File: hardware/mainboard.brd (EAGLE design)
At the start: 160 x 100 mm, 86 parts, among them IC1 ATMEGA328, IC10 HM628512A_DIL32, IC11 HM628512A_DIL32, IC12 7805TV, IC14 6N138, IC3 TL974, IC4 74HCT04N, IC5 74HC238N, IC6 74HCT573N, IC7 74HCT573N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

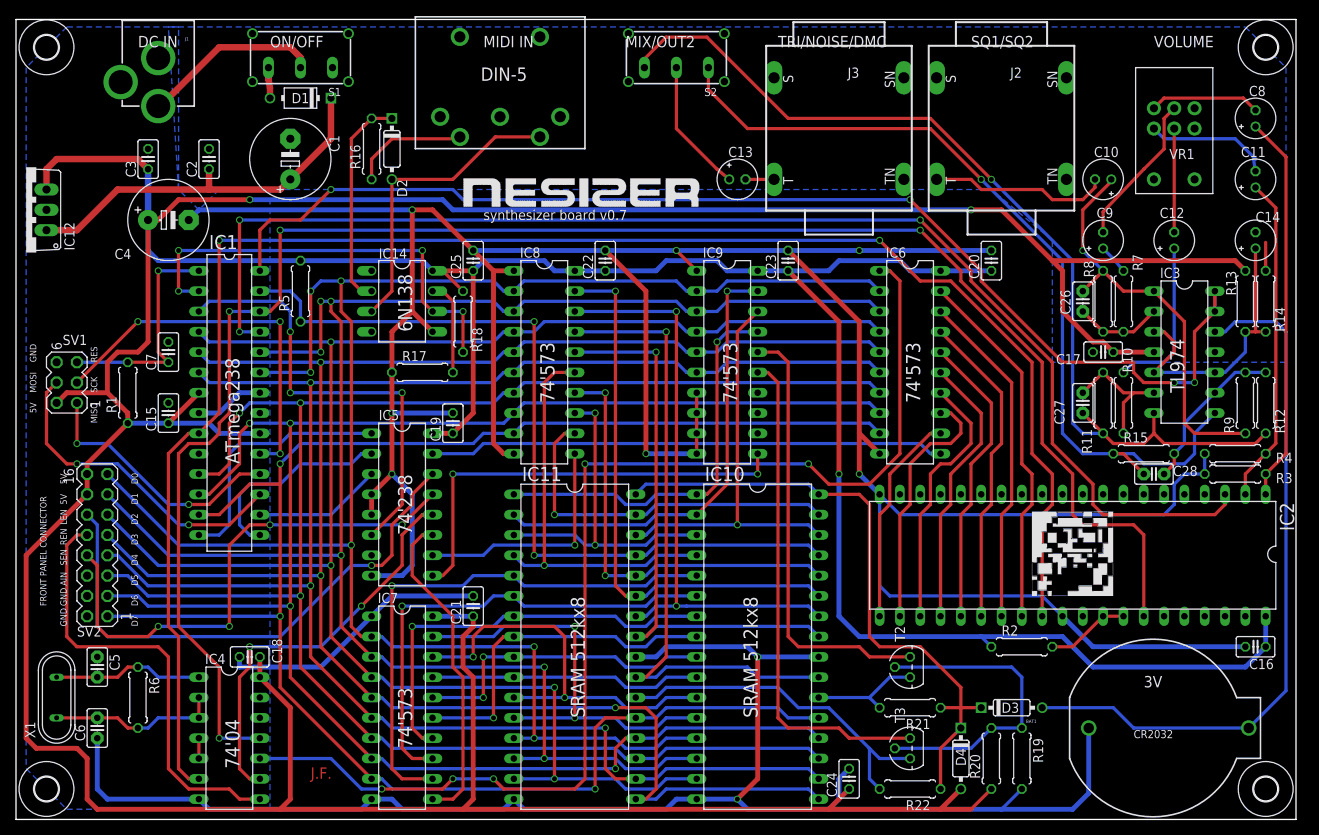
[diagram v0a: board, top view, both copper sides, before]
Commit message: Main board v0.9: fix memory backup, new MIDI connector, BOM fixes
The discrete memory backup circuit turned out to be too fragile. The old
DS1210 based design is back, but it is now also used to provide the CPU
RESET signal to further reduce the possibility of memory corruption. The
battery voltage is still being connected (through a buffer) to the
Atmega for being able to check the battery voltage.

The MIDI connector that was used previously is not being stocked at
Mouser any more, so it has been replaced by one that is.

A couple of fixes have been done to the BOM, replacing out of stock
components with drop-in replacements (a resistor and the 74'238).

This should hopefully be the last revision of the main board...
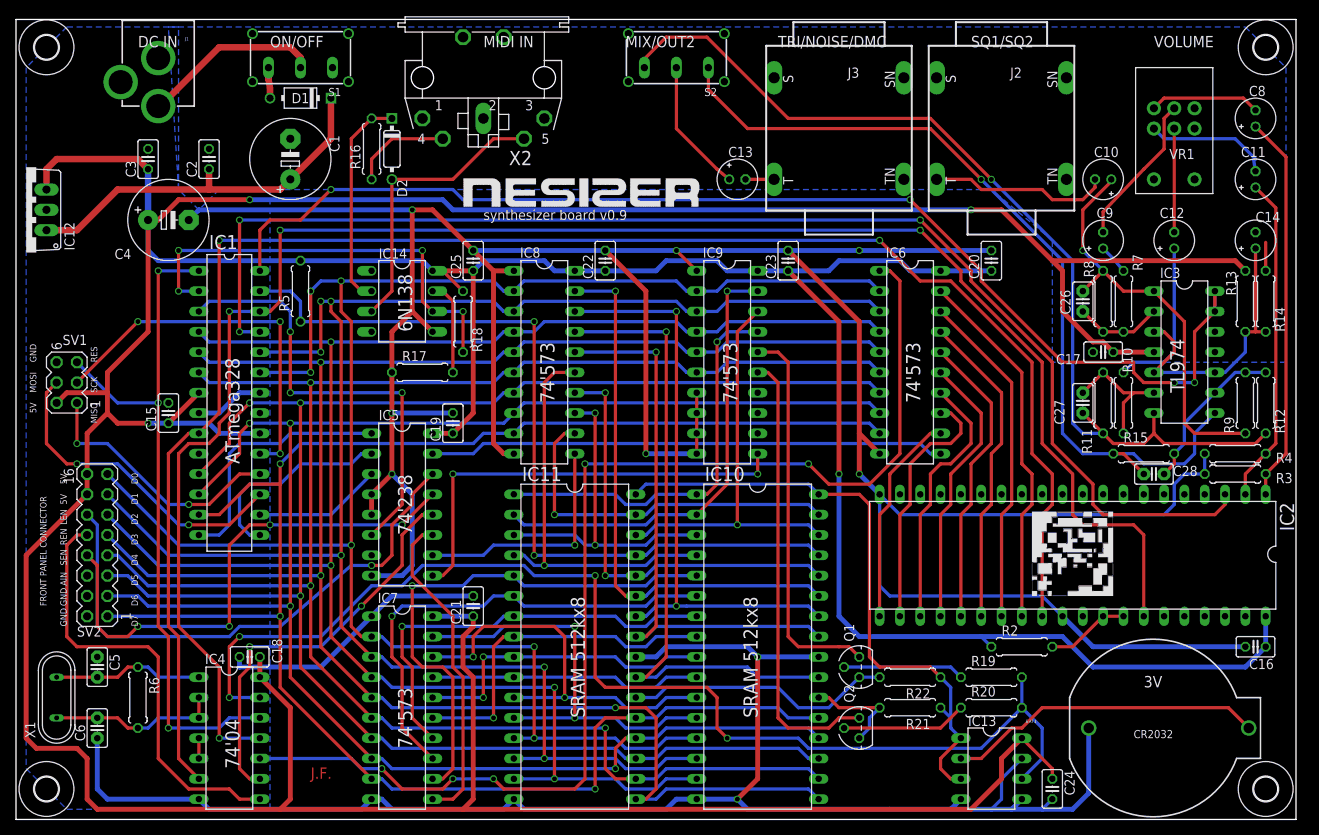
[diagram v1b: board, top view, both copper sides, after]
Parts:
- removed C7: 10n, rcl:C025-025X050
- removed D3, D4: 1N914.3, gm-diodes:DO35-3
- removed J4: MIDI_CONN_FEMALE_SUPPORT, SparkFun-Connectors:DIN_5_FEMALE_SUPPORT
- removed R1: 4.7k, rcl:0207/7
- removed T2, T3: BC547, transistor:TO92
- added IC13: DS1210-8PDIP, maxim-custom:DIL08
- added Q1, Q2: BC557, transistor-pnp:TO92
- added X2: MAB5SH, con-hirschmann:MAB5SH
- R19: value 4.7k -> 1k
- R20: value 27k -> 1k
- R21, R22: value 4.7k -> 100k
- moved C24 25.4 mm to (129.5, 3.81), turned to 270 degrees
- moved R22 14.0 mm to (111.8, 17.8)
- moved R19 10.9 mm to (121.9, 17.8), turned to 0 degrees
- moved R20 6.35 mm to (121.9, 14.0), turned to 0 degrees
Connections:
- removed net N$19: BAT1.1, D3.A, IC3.12
- new net N$37: Q1.2, R19.1
- new net N$38: Q2.2, R20.1
- new net N$39: BAT1.1, IC13.2, IC3.12
- net CE1: now also Q1.1; no longer T2.1
- net CE2: now also Q2.1; no longer T3.1
- net GND: now also IC13.4, IC13.5, IC13.7, X2.PE, X2.PE@; no longer C7.2, IC4.13, R19.2
- net MEM1_CE: now also Q2.3; no longer T2.3
- net MEM2_CE: now also Q1.3; no longer T3.3
- net MEM_VCC: now also IC13.1, IC13.3; no longer D3.C, D4.C
- net MIDI_PIN_4: now also X2.4; no longer J4.4
- net MIDI_PIN_5: now also X2.5; no longer J4.5
- net N$33: now also IC13.6, IC4.13, R19.2; no longer R19.1, T2.2, T3.2
- net RESET: now also IC4.12; no longer C7.1, R1.2
- net VCC: now also IC13.8; no longer D4.A, R1.1, R20.1
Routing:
- net N$33: track 39.7 -> 149.5 mm, vias 0 -> 4
- net N$19: track 88.3 -> 0.00 mm
- net RESET: track 28.5 -> 87.0 mm, vias 1 -> 3
- net N$39: track 0.00 -> 39.7 mm
- net N$38: track 0.00 -> 15.7 mm
- net N$37: track 0.00 -> 15.1 mm
- net MEM2_CE: track 44.1 -> 33.6 mm
- net VCC: track 727.0 -> 733.9 mm, vias 3 -> 4
- net CE2: track 62.5 -> 56.2 mm
- net CE1: track 54.9 -> 48.6 mm
- net GND: track 637.6 -> 641.2 mm
- net MIDI_PIN_4: track 14.7 -> 12.5 mm
- net MIDI_PIN_5: track 38.3 -> 36.2 mm
- net MEM_VCC: track 80.2 -> 78.2 mm
- net DB5: track 222.1 -> 220.6 mm
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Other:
- board text added: "ATmega328"
- board text added: "synthesizer board v0.9"
- board text removed: "ATmega238"
- board text removed: "synthesizer board v0.7"

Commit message: HW 0.9 fix
Added missing trace from battery to op-amp
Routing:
- net N$39: track 39.7 -> 88.1 mm, vias 0 -> 2
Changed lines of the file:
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@@
 <wire x1="128.27" y1="13.97" x2="151.55" y2="13.97" width="0.4064" layer="1"/>
 <wire x1="151.55" y1="13.97" x2="154.09" y2="11.43" width="0.4064" layer="1"/>
-<wire x1="151.55" y1="13.97" x2="149.86" y2="60.96" width="0" layer="19" extent="1-1"/>
+<wire x1="151.55" y1="13.97" x2="151.55" y2="22.01" width="0.4064" layer="1"/>
+<wire x1="151.55" y1="22.01" x2="152.4" y2="22.86" width="0.4064" layer="1"/>
+<wire x1="152.4" y1="22.86" x2="152.4" y2="45.72" width="0.4064" layer="1"/>
+<via x="152.4" y="45.72" extent="1-16" drill="0.6"/>
+<wire x1="152.4" y1="45.72" x2="152.4" y2="49.53" width="0.4064" layer="16"/>
+<via x="152.4" y="49.53" extent="1-16" drill="0.6"/>
+<wire x1="152.4" y1="49.53" x2="152.4" y2="58.42" width="0.4064" layer="1"/>
+<wire x1="152.4" y1="58.42" x2="149.86" y2="60.96" width="0.4064" layer="1"/>
 </signal>
 </signals>

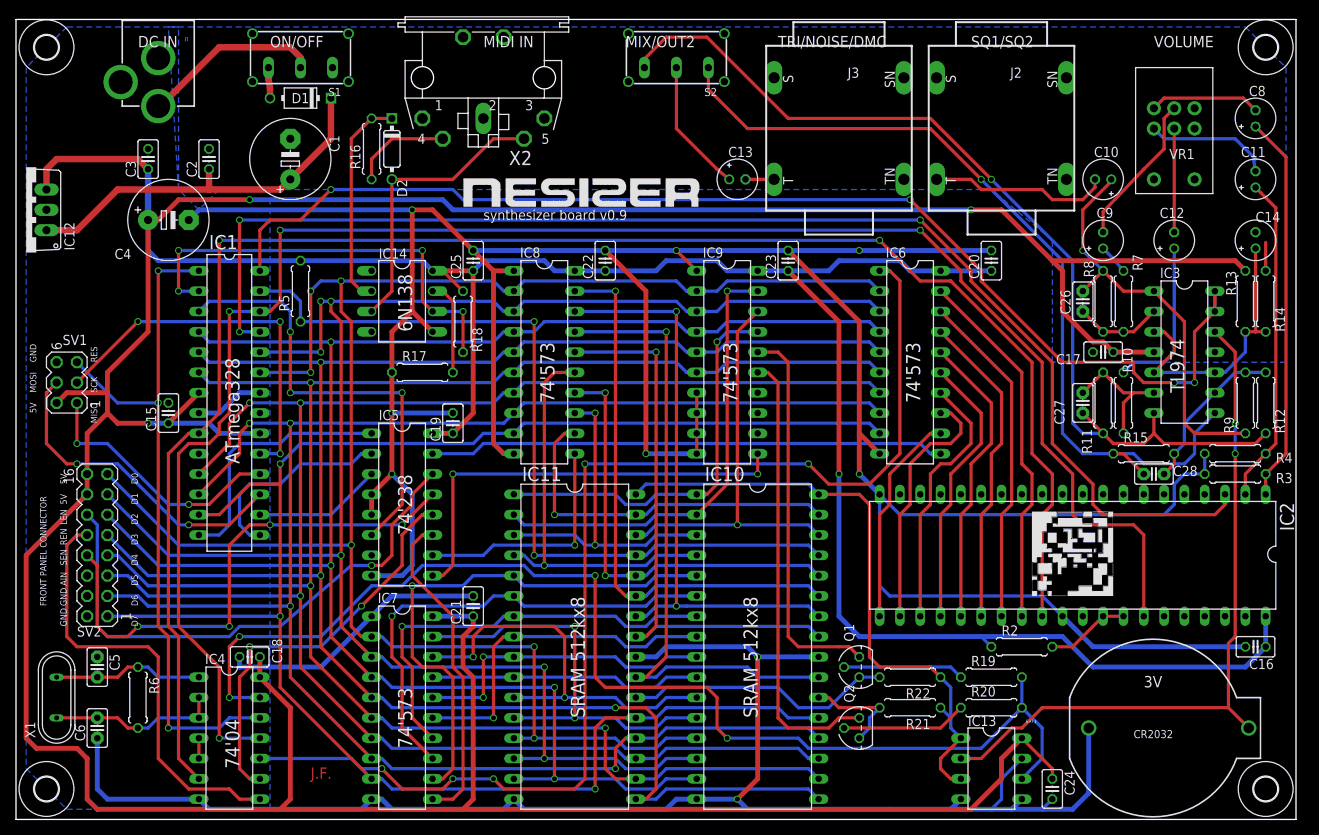
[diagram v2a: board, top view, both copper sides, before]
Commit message: HW: main board update
Fixes a few faults in the latest main board revision:

- Remove RESET connection from DS1210
- Add 10M resistor between battery and op-amp
        Eliminates leakage through op-amp inputs which would
        cause DS1210 to switch mode to "on".
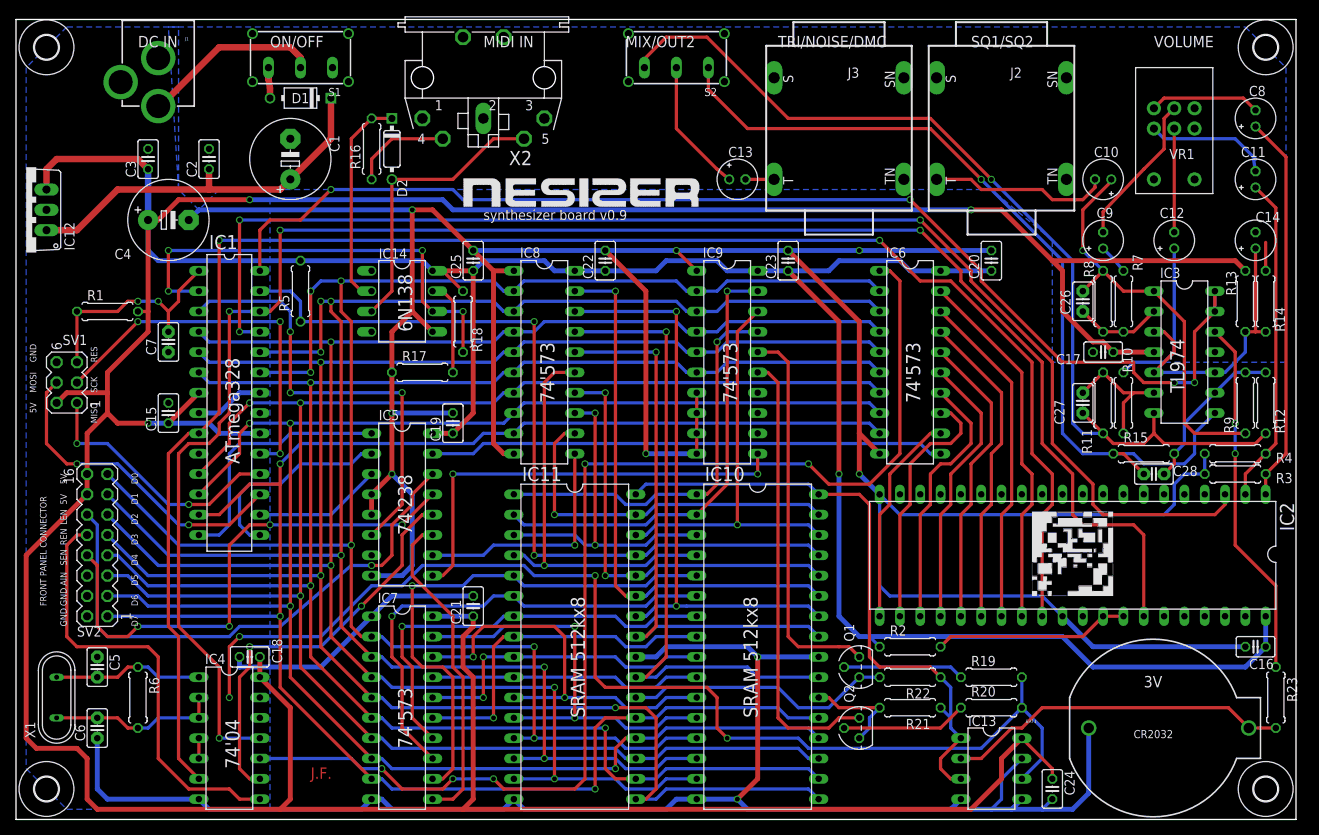
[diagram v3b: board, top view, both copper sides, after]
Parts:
- added C7: 10n, capacitor-wima:C2.5-2
- added R1: 4.7k, rcl:0207/7
- added R23: 10M, rcl:0207/7
- IC3: value TL974 -> TLC074
- R19, R20: value 1k -> 4.7k
- moved R2 14.0 mm to (111.8, 21.6)
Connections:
- new net N$19: IC3.12, R23.1
- net GND: now also C7.1, IC4.13
- net N$33: no longer IC4.13
- net N$39: now also R23.2; no longer IC3.12
- net RESET: now also C7.2, R1.1; no longer IC4.12
- net VCC: now also R1.2
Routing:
- net RESET: track 87.0 -> 28.0 mm, vias 3 -> 2
- net N$19: track 0.00 -> 45.1 mm, vias 0 -> 2
- net N$39: track 88.1 -> 43.1 mm, vias 2 -> 0
- net N$16: track 10.5 -> 24.4 mm
- net N$33: track 149.5 -> 145.7 mm
- net MIDI_IN: track 55.1 -> 57.7 mm
- net VCC: track 733.9 -> 735.2 mm

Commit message: mainboard v0.95: fixes and MIDI out
Fixed faults with battery measurement and RESET circuitry.

Added MIDI OUT connector.
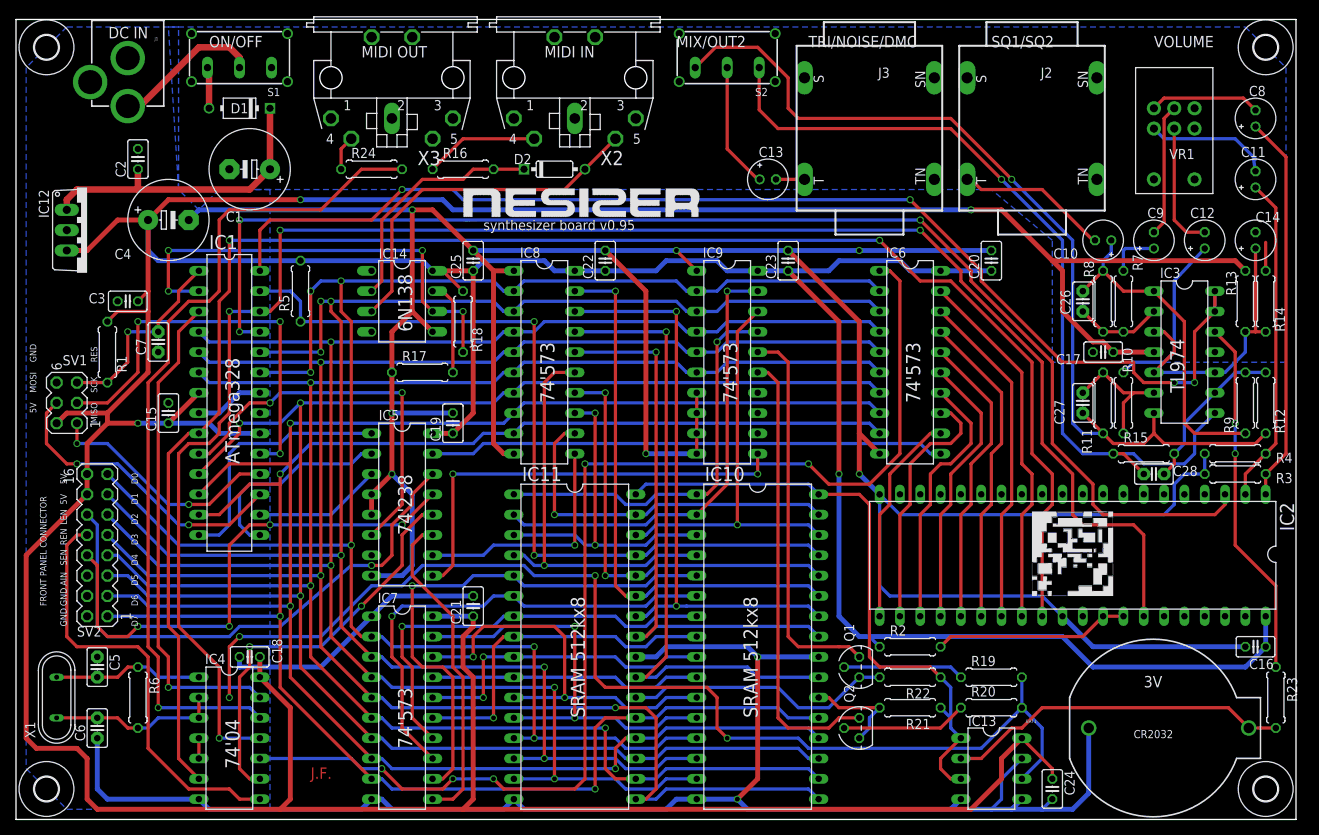
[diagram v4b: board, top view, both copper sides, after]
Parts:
- added R24: 220, rcl:0207/7
- added X3: MAB5SH, con-hirschmann:MAB5SH
- moved D2 20.5 mm to (67.3, 81.3), turned to 0 degrees
- moved C3 18.0 mm to (14.0, 64.8), turned to 180 degrees
- moved R16 11.7 mm to (55.9, 81.3), turned to 0 degrees
- moved X2 11.4 mm to (69.8, 92.7)
- moved C2 8.89 mm to (15.2, 82.5)
- moved IC12 8.03 mm to (8.89, 73.7), turned to 270 degrees
- moved D1 7.73 mm to (27.9, 88.9)
- moved C10 7.62 mm to (135.9, 72.4)
- moved S1 7.62 mm to (27.9, 94.0)
- moved C9 6.35 mm to (142.2, 72.4)
- moved S2 6.35 mm to (88.9, 94.0)
- moved C1 5.24 mm to (29.2, 81.3), turned to 180 degrees
- moved R1 5.08 mm to (11.4, 58.4), turned to 90 degrees
- moved C12 3.81 mm to (148.6, 72.4)
- moved C13 3.81 mm to (94.0, 80.0)
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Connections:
- new net MIDI_OUT: IC1.3, IC4.13
- new net N$40: IC4.12, R24.2
- new net N$41: R24.1, X3.4
- net BUS_EN: now also IC1.10; no longer IC1.3
- net GND: now also X3.2, X3.5, X3.PE, X3.PE@; no longer IC4.13
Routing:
- net N$40: track 0.00 -> 105.4 mm, vias 0 -> 1
- net MIDI_OUT: track 0.00 -> 61.6 mm, vias 0 -> 1
- net N$35: track 47.9 -> 38.4 mm
- net N$25: track 50.9 -> 41.5 mm, vias 1 -> 0
- net MIDI_PIN_5: track 36.2 -> 44.6 mm
- net BUS_EN: track 56.0 -> 48.7 mm, vias 3 -> 2
- net VCC: track 735.2 -> 729.9 mm
- net SCK: track 47.6 -> 52.4 mm
- net N$41: track 0.00 -> 4.34 mm
- net N$31: track 23.0 -> 18.8 mm
- net DB6: track 221.9 -> 218.3 mm, vias 4 -> 3
- net N$26: track 107.1 -> 103.7 mm
- net RESET: track 28.0 -> 24.7 mm, vias 2 -> 1
- net N$36: track 119.4 -> 116.2 mm
- net N$22: track 22.5 -> 19.5 mm
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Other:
- board text added: "MIDI OUT"
- board text added: "synthesizer board v0.95"
- board text removed: "synthesizer board v0.9"
